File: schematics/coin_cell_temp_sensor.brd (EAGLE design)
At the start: 4 parts

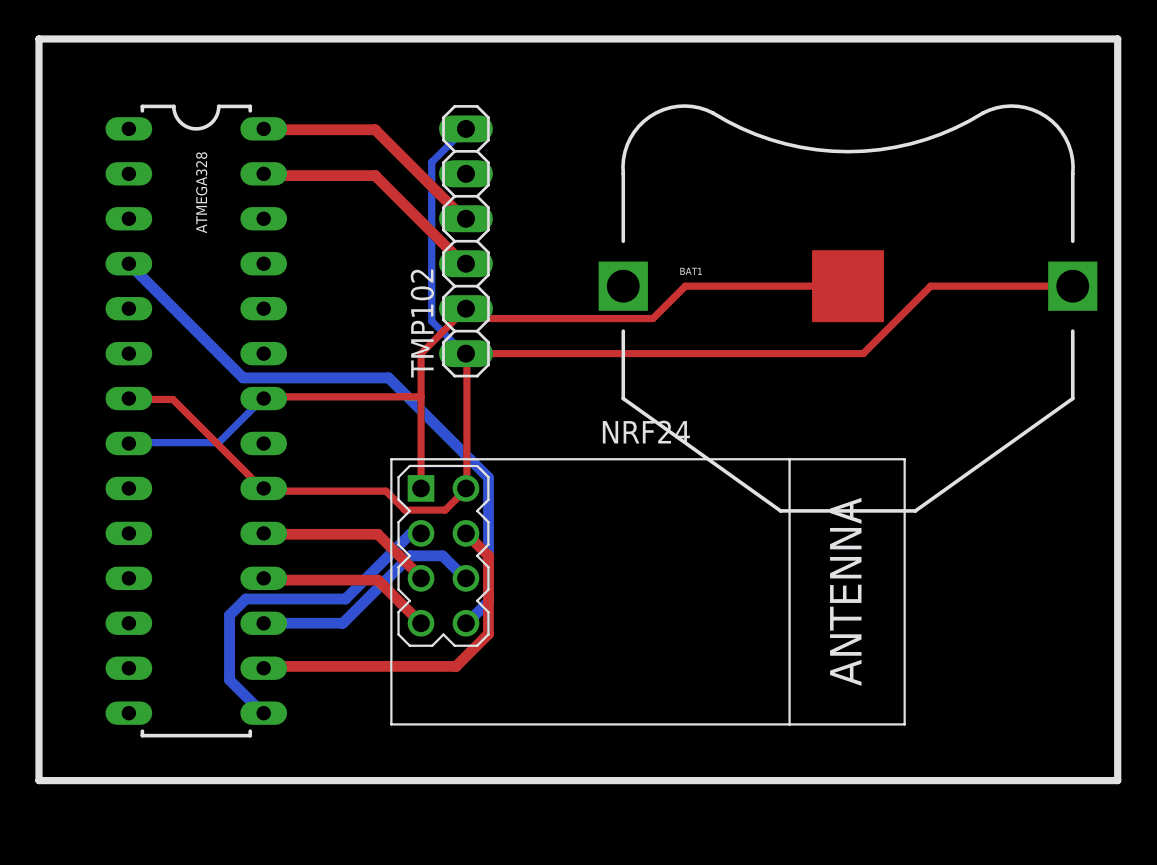
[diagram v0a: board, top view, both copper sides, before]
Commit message: Updated the schematics with a routed PCB board
Added a gitignore file.

Added a fritzing schematic of the breadboard.
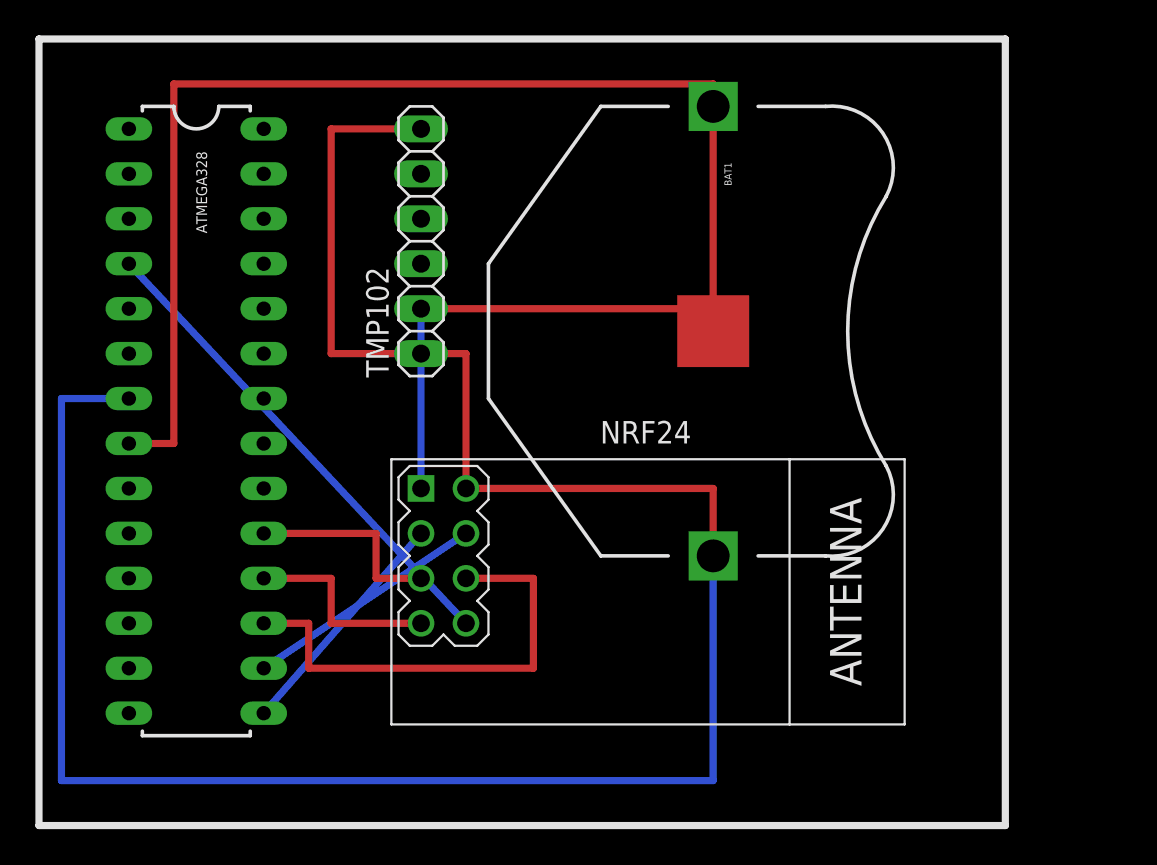
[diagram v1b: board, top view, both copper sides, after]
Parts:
- moved BAT1 8.03 mm to (43.2, 62.2), turned to 270 degrees
- moved TMP102 2.54 mm to (26.7, 67.3)
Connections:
- net SCL: no longer ATMEGA328.28
- net SDA: no longer ATMEGA328.27
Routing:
- net VCC: track 80.2 -> 125.7 mm
- net GND: track 51.4 -> 95.2 mm
- net SDA: track 13.6 -> 0.00 mm
- net SCL: track 13.5 -> 0.00 mm
- net MOSI: track 13.5 -> 26.7 mm
- net IRQ: track 34.1 -> 27.9 mm
- net CSN: track 19.7 -> 13.7 mm
- net CE: track 19.1 -> 13.5 mm
- net MISO: track 9.96 -> 11.4 mm
- net SCK: track 9.97 -> 11.4 mm
